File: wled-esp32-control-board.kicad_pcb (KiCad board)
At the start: 4 copper layers, 64.9 x 39.5 mm, 55 parts, among them J101 Conn_01x03, J102 Conn_01x03, J103 Conn_01x03, J104 Conn_01x03, J105 Conn_02x03_Odd_Even, J201 USB_C_Receptacle_USB2.0, Q401 MMDT3904, SW101 SW_SPDT, SW103 SW_Push, SW105 SW_Push, U101 74AHCT1G125, U102 74AHCT1G125, U103 ESP32-WROOM-32, U104 74AHCT1G125, U105 74AHCT1G125, U106 TSOP382xx, U301 XC6220B331MR-G, U401 CP2102-GMR

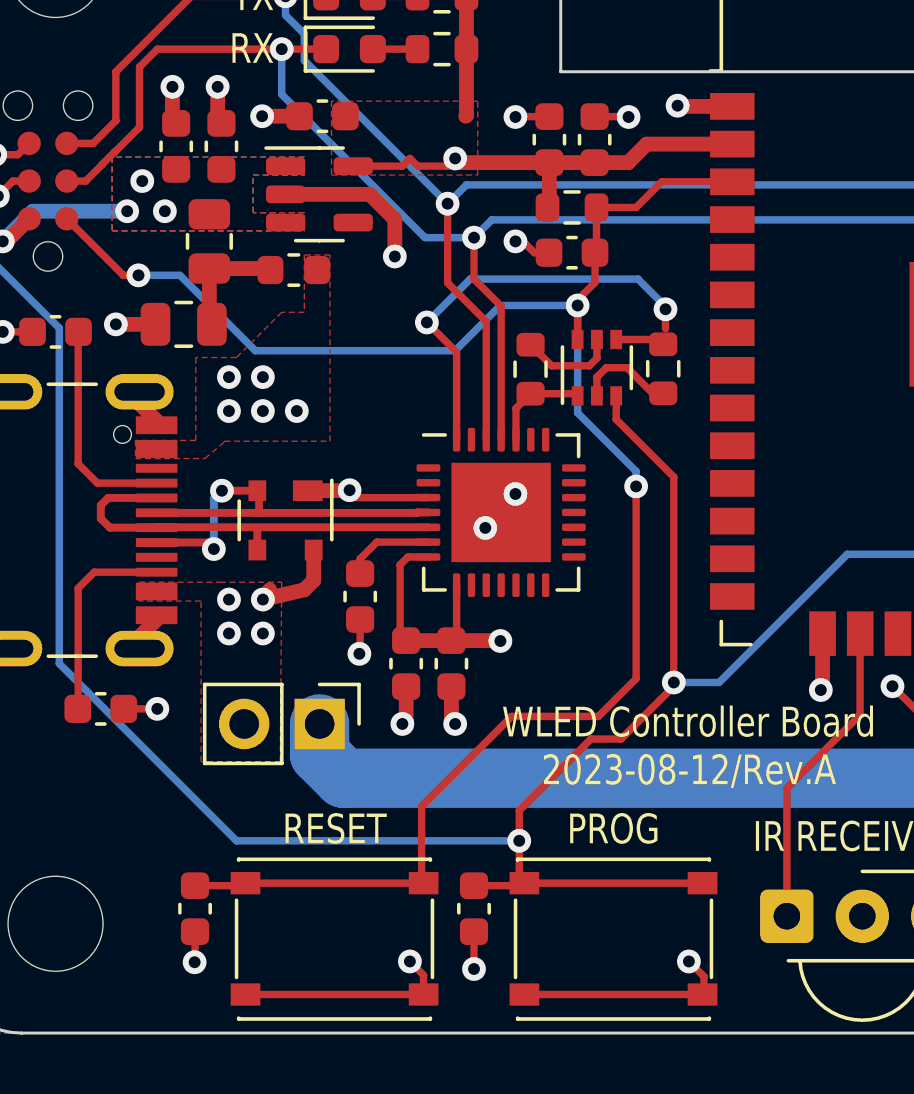
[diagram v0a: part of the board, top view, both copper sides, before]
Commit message: reposition cap near EN pin
Cap repositioned near EN pin. Rev.A does not boot at power on, forcing to press reset button to boot up properly.

Tactile button caps were removed.
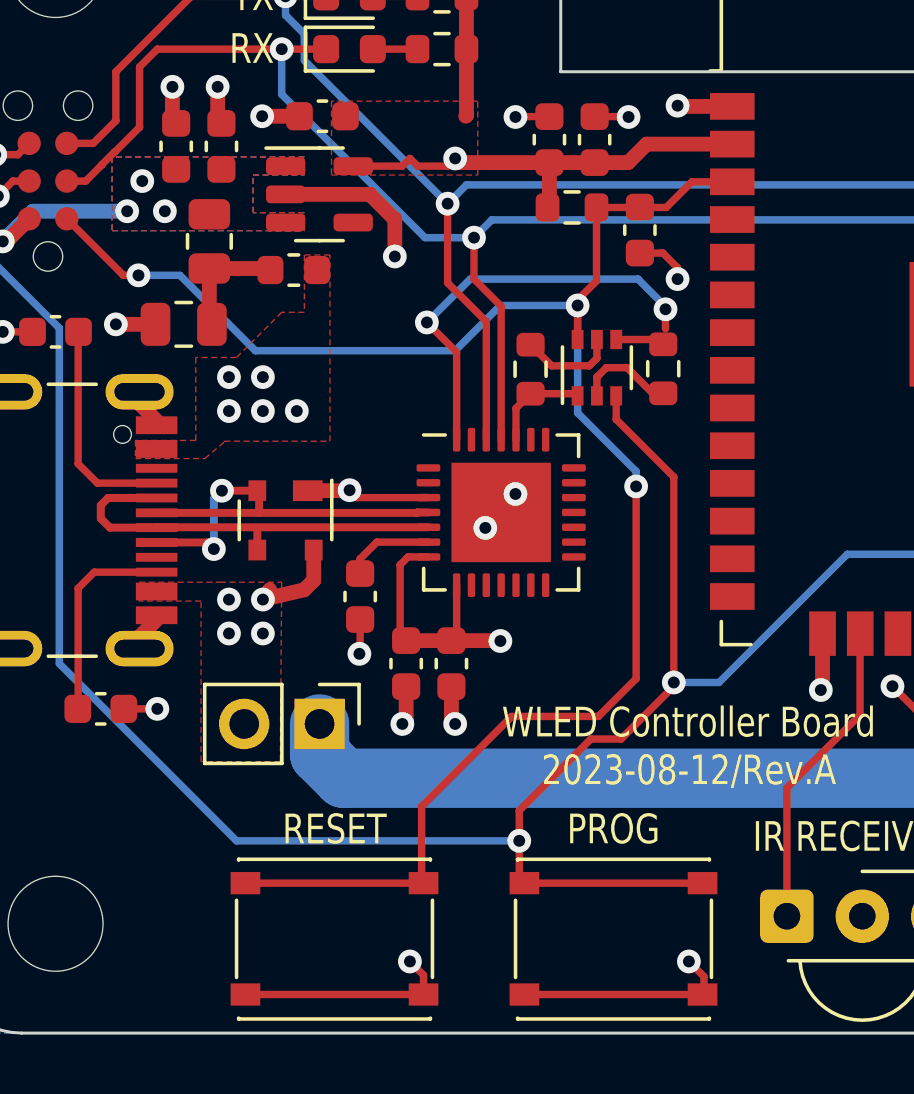
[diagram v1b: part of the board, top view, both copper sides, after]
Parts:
- removed C106, C107: 100nF, Capacitor_SMD:C_0603_1608Metric
- moved C104 2.41 mm to (121.3, 80.9), turned to -90 degrees
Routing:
- net GND: track 62.9 -> 61.2 mm, vias 35 -> 33
- net /IO0: track 87.5 -> 85.8 mm
- net /EN: track 62.1 -> 60.5 mm

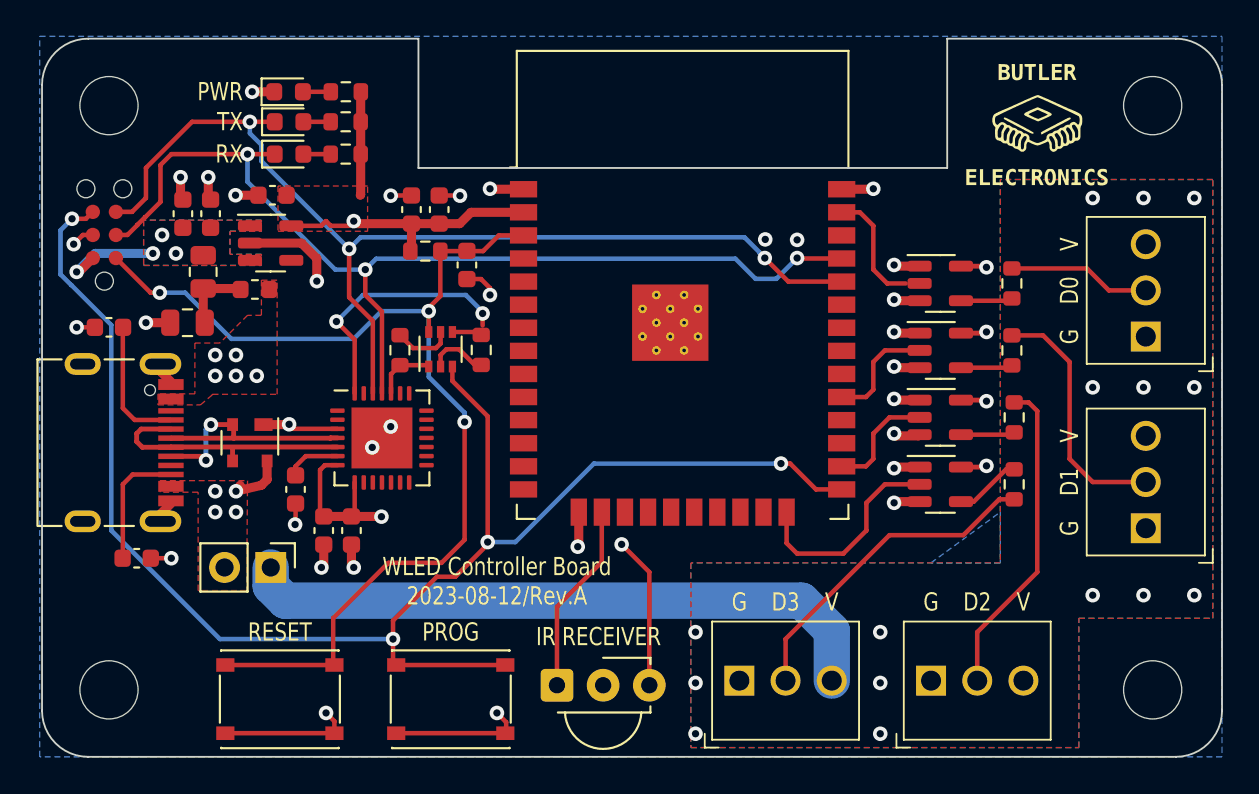
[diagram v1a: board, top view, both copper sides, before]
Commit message: update silkscreen labels and revision
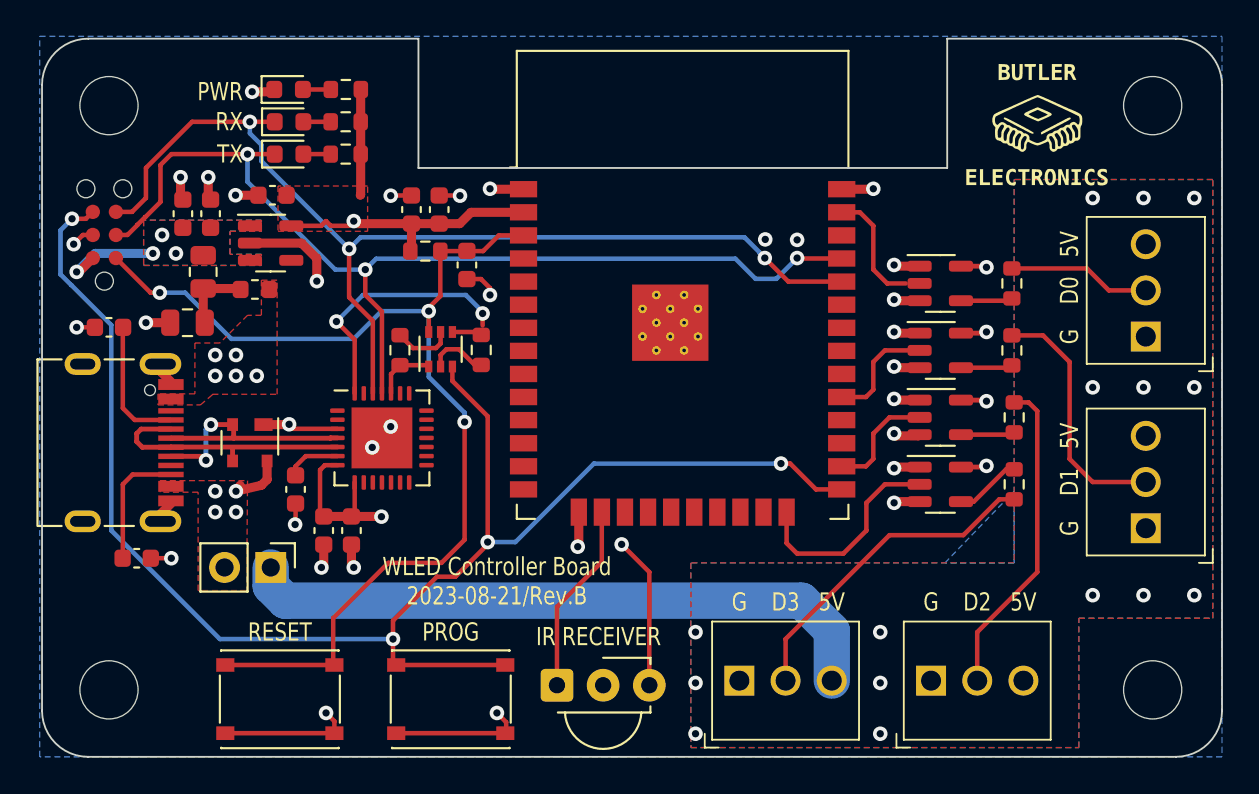
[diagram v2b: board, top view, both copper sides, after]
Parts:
- moved LED103 0.13 mm to (111.5, 71.2)
- moved R107 0.13 mm to (114.6, 71.2)
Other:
- board text added: "5V"
- board text removed: "V"
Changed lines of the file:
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@@
   (title_block
     (title "WLED Controller Board")
-    (date "2023-08-12")
-    (rev "A")
+    (date "2023-08-21")
+    (rev "B")
     (company "Bulter Electronics")
   )
@@
   )
   (footprint "Resistor_SMD:R_0603_1608Metric" (layer "F.Cu")
-    (at 114.627 71.374 180)
+    (at 114.627 71.247 180)
     (descr "Resistor SMD 0603 (1608 Metric), square (rectangular) end terminal, IPC_7351 nominal, (Body size source: IPC-SM-782 page 72, https://www.pcb-3d.com/wordpress/wp-content/uploads/ipc-sm-782a_amendment_1_and_2.pdf), generated with kicad-footprint-generator")
     (tags "resistor")
@@
   )
   (footprint "LED_SMD:LED_0603_1608Metric" (layer "F.Cu")
-    (at 111.4775 71.374)
+    (at 111.4775 71.247)
     (descr "LED SMD 0603 (1608 Metric), square (rectangular) end terminal, IPC_7351 nominal, (Body size source: http://www.tortai-tech.com/upload/download/2011102023233369053.pdf), generated with kicad-footprint-generator")
     (tags "LED")
@@
     (effects (font (size 1 0.8) (thickness 0.2) bold) (justify left mirror))
   )
-  (gr_text "V" (at 154.432 79.756 90) (layer "F.SilkS")
+  (gr_text "5V" (at 154.432 79.756 90) (layer "F.SilkS")
     (effects (font (size 1 0.8) (thickness 0.153)))
   )
@@
     (effects (font (size 1 0.8) (thickness 0.153)))
   )
-  (gr_text "V" (at 151.892 99.441) (layer "F.SilkS")
+  (gr_text "5V" (at 151.892 99.441) (layer "F.SilkS")
     (effects (font (size 1 0.8) (thickness 0.153)))
   )
@@
     (effects (font (size 1 0.8) (thickness 0.153)))
   )
-  (gr_text "TX" (at 108.966 73.025) (layer "F.SilkS")
+  (gr_text "RX" (at 108.966 73.025) (layer "F.SilkS")
     (effects (font (size 1 0.8) (thickness 0.153)) (justify right))
   )
@@
     (effects (font (size 1 0.8) (thickness 0.153)))
   )
-  (gr_text "V" (at 154.432 90.297 90) (layer "F.SilkS")
+  (gr_text "5V" (at 154.432 90.297 90) (layer "F.SilkS")
     (effects (font (size 1 0.8) (thickness 0.153)))
   )
@@
     (effects (font (size 1 0.8) (thickness 0.153)))
   )
-  (gr_text "RX" (at 108.966 74.803) (layer "F.SilkS")
+  (gr_text "TX" (at 108.966 74.803) (layer "F.SilkS")
     (effects (font (size 1 0.8) (thickness 0.153)) (justify right))
   )
-  (gr_text "V" (at 141.351 99.441) (layer "F.SilkS")
+  (gr_text "5V" (at 141.351 99.441) (layer "F.SilkS")
     (effects (font (size 1 0.8) (thickness 0.153)))
   )
@@
   (segment (start 99.822 81.28) (end 100.838 80.264) (width 0.5) (layer "B.Cu") (net 3))
   (segment (start 113.932 100.317) (end 116.967 97.282) (width 0.25) (layer "F.Cu") (net 4))
-  (segment (start 107.914 102.984) (end 107.998 102.9) (width 0.25) (layer "F.Cu") (net 4))
   (segment (start 119.824 80.187) (end 119.824 82.614) (width 0.25) (layer "F.Cu") (net 4))
   (segment (start 119.824 82.614) (end 119.1872 83.2508) (width 0.25) (layer "F.Cu") (net 4))
@@
   (segment (start 117.396 102.9) (end 123.396 102.9) (width 0.25) (layer "F.Cu") (net 5))
   (segment (start 120.4872 87.277404) (end 120.4872 86.485204) (width 0.25) (layer "F.Cu") (net 5))
-  (segment (start 117.312 102.984) (end 117.396 102.9) (width 0.25) (layer "F.Cu") (net 5))
   (segment (start 117.221 100.457) (end 119.634 98.044) (width 0.25) (layer "F.Cu") (net 5))
   (via (at 117.221 101.473) (size 0.8) (drill 0.4) (layers "F.Cu" "B.Cu") (net 5))
@@
   (segment (start 102.362 88.773) (end 102.362 84.468) (width 0.25) (layer "F.Cu") (net 16))
   (segment (start 105.006 89.423) (end 103.012 89.423) (width 0.25) (layer "F.Cu") (net 16))
-  (segment (start 102.362 84.468) (end 102.108 84.214) (width 0.25) (layer "F.Cu") (net 16))
   (segment (start 103.012 89.423) (end 102.362 88.773) (width 0.25) (layer "F.Cu") (net 16))
   (segment (start 102.362 97.015) (end 102.362 92.964) (width 0.25) (layer "F.Cu") (net 18))
@@
   (segment (start 109.347 73.66) (end 109.347 73.025) (width 0.25) (layer "B.Cu") (net 22))
   (segment (start 113.793 73.025) (end 112.29 73.025) (width 0.25) (layer "F.Cu") (net 23))
-  (segment (start 113.802 71.374) (end 112.265 71.374) (width 0.25) (layer "F.Cu") (net 24))
+  (segment (start 113.802 71.247) (end 112.265 71.247) (width 0.25) (layer "F.Cu") (net 24))
   (segment (start 117.602 86.411004) (end 119.113 86.411004) (width 0.25) (layer "F.Cu") (net 25))
   (segment (start 119.113 86.411004) (end 119.1872 86.485204) (width 0.25) (layer "F.Cu") (net 25))
@@
       (pts
         (xy 162.306 76.2)
-        (xy 150.622 76.2)
-        (xy 150.622 97.282)
+        (xy 151.384 76.2)
+        (xy 151.384 97.282)
         (xy 133.604 97.282)
         (xy 133.604 107.442)
@@
     (polygon
       (pts
-        (xy 146.812 97.282)
-        (xy 150.622 94.488)
-        (xy 150.622 97.282)
+        (xy 147.574 97.282)
+        (xy 151.384 93.345)
+        (xy 151.384 97.282)
       )
     )

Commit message: update silkscreen and routing
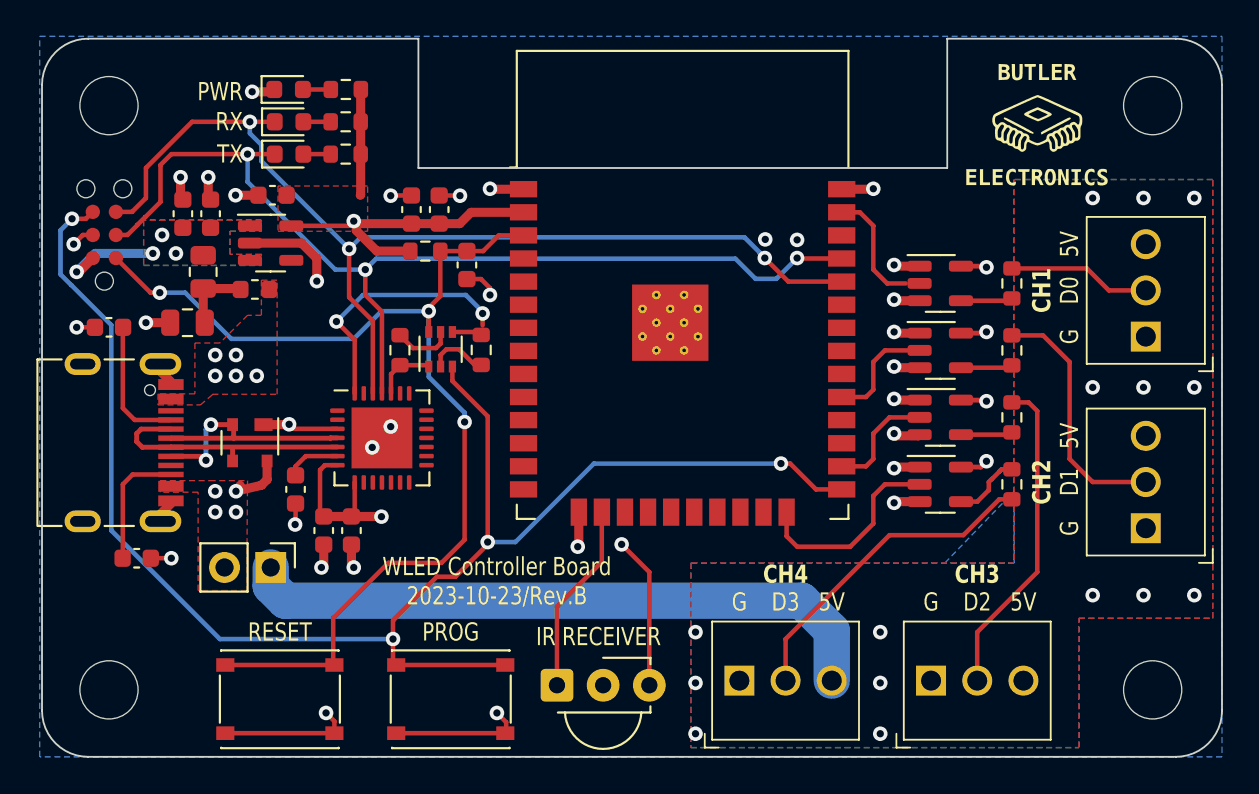
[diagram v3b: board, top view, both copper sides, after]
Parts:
- moved R106 0.13 mm to (151.3, 89.3)
- moved R108 0.13 mm to (151.3, 93.0)
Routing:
- net +3.3V: track 56.0 -> 58.1 mm
- net /LED3: track 11.7 -> 11.2 mm
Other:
- board text added: "CH1"
- board text added: "CH2"
- board text added: "CH3"
- board text added: "CH4"
- board text added: "WLED CHANNELS"
